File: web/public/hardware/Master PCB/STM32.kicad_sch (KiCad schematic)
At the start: 18 parts, among them SW1 nRST, U1 STM32U585VITx

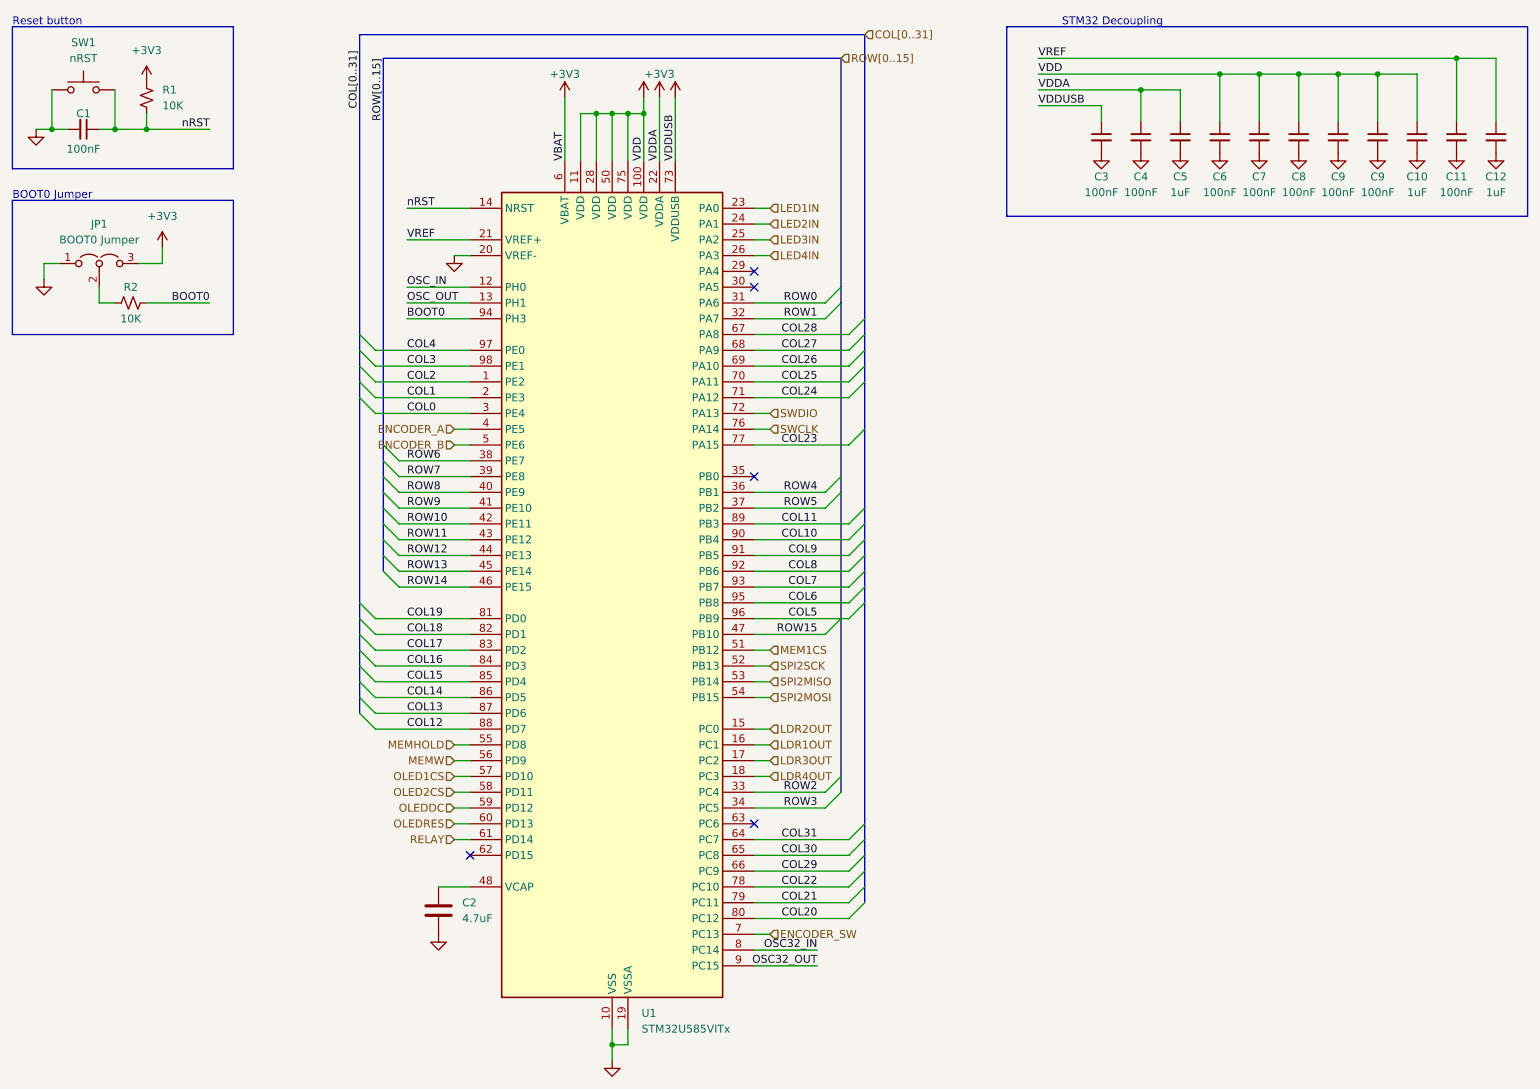
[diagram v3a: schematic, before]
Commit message: Change STM32 pinout, begin placing components on new PCB
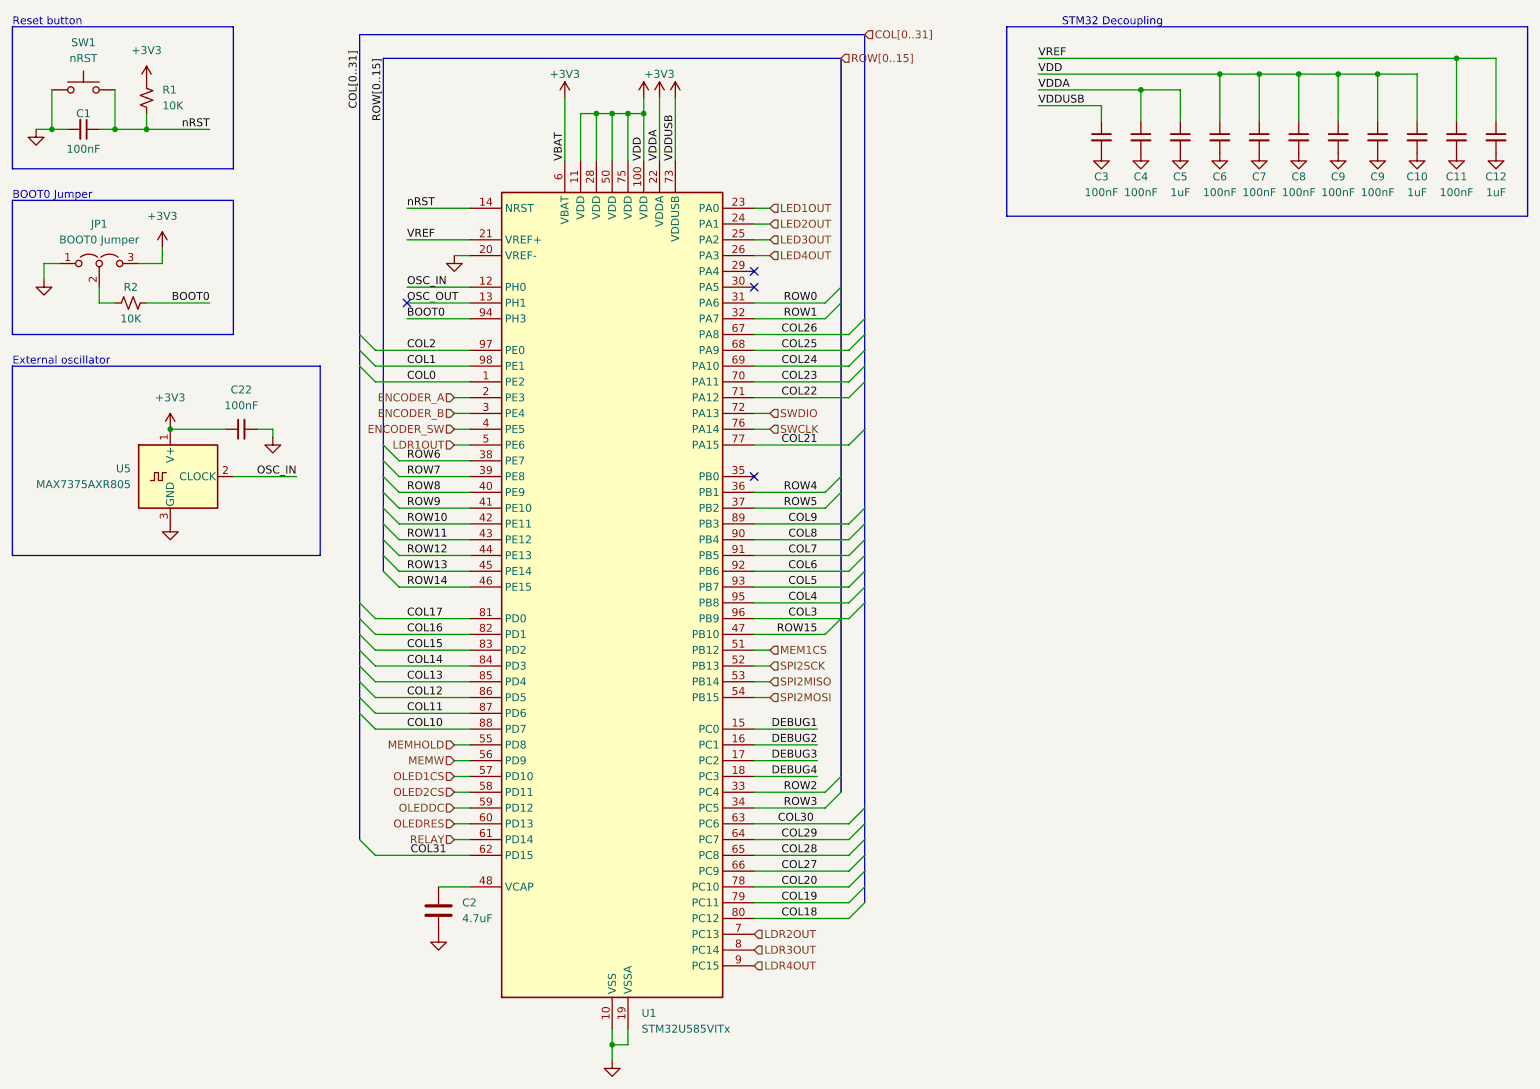
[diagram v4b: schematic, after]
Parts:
- added C22: 100nF, Capacitor_SMD:C_0805_2012Metric_Pad1.18x1.45mm_HandSolder, symbol Device:C_Small
- added U5: MAX7375AXR805, Package_TO_SOT_SMD:SOT-323_SC-70, symbol Oscillator:MAX7375AXR805
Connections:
- net OSC32_IN is gone; now on net LDR3OUT: U1.8 (PC14)
- net OSC32_OUT is gone; now on net LDR4OUT: U1.9 (PC15)
- net +3V3: now also C22.1, U5.1 (V+)
- net COL0: now also U1.1 (PE2); no longer U1.3 (PE4)
- net COL1: now also U1.98 (PE1); no longer U1.2 (PE3)
- net COL10: now also U1.88 (PD7); no longer U1.90 (PB4)
- net COL11: now also U1.87 (PD6); no longer U1.89 (PB3)
- net COL12: now also U1.86 (PD5); no longer U1.88 (PD7)
- net COL13: now also U1.85 (PD4); no longer U1.87 (PD6)
- net COL14: now also U1.84 (PD3); no longer U1.86 (PD5)
- net COL15: now also U1.83 (PD2); no longer U1.85 (PD4)
- net COL16: now also U1.82 (PD1); no longer U1.84 (PD3)
- net COL17: now also U1.81 (PD0); no longer U1.83 (PD2)
- net COL18: now also U1.80 (PC12); no longer U1.82 (PD1)
- net COL19: now also U1.79 (PC11); no longer U1.81 (PD0)
- net COL2: now also U1.97 (PE0); no longer U1.1 (PE2)
- net COL20: now also U1.78 (PC10); no longer U1.80 (PC12)
- net COL21: now also U1.77 (PA15); no longer U1.79 (PC11)
- net COL22: now also U1.71 (PA12); no longer U1.78 (PC10)
- net COL23: now also U1.70 (PA11); no longer U1.77 (PA15)
- net COL24: now also U1.69 (PA10); no longer U1.71 (PA12)
- net COL25: now also U1.68 (PA9); no longer U1.70 (PA11)
- net COL26: now also U1.67 (PA8); no longer U1.69 (PA10)
- net COL27: now also U1.66 (PC9); no longer U1.68 (PA9)
- net COL28: now also U1.65 (PC8); no longer U1.67 (PA8)
- net COL29: now also U1.64 (PC7); no longer U1.66 (PC9)
- net COL3: now also U1.96 (PB9); no longer U1.98 (PE1)
- net COL30: now also U1.63 (PC6); no longer U1.65 (PC8)
- net COL31: now also U1.62 (PD15); no longer U1.64 (PC7)
- net COL4: now also U1.95 (PB8); no longer U1.97 (PE0)
- net COL5: now also U1.93 (PB7); no longer U1.96 (PB9)
- net COL6: now also U1.92 (PB6); no longer U1.95 (PB8)
- net COL7: now also U1.91 (PB5); no longer U1.93 (PB7)
- net COL8: now also U1.90 (PB4); no longer U1.92 (PB6)
- net COL9: now also U1.89 (PB3); no longer U1.91 (PB5)
- net ENCODER_A: now also U1.2 (PE3); no longer U1.4 (PE5)
- net ENCODER_B: now also U1.3 (PE4); no longer U1.5 (PE6)
- net ENCODER_SW: now also U1.4 (PE5); no longer U1.7 (PC13)
- net GND: now also C22.2, U5.3 (GND)
- net LDR1OUT: now also U1.5 (PE6); no longer U1.16 (PC1)
- net LDR2OUT: now also U1.7 (PC13); no longer U1.15 (PC0)
- net LDR3OUT: no longer U1.17 (PC2)
- net LDR4OUT: no longer U1.18 (PC3)
- net OSC_IN: now also U5.2 (CLOCK)
- net LED1IN renamed LED1OUT
- net LED2IN renamed LED2OUT
- net LED3IN renamed LED3OUT
- net LED4IN renamed LED4OUT
- new net DEBUG1: U1.15 (PC0)
- new net DEBUG2: U1.16 (PC1)
- new net DEBUG3: U1.17 (PC2)
- new net DEBUG4: U1.18 (PC3)
- no-connect marks 5 -> 4
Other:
- note added: "External oscillator"

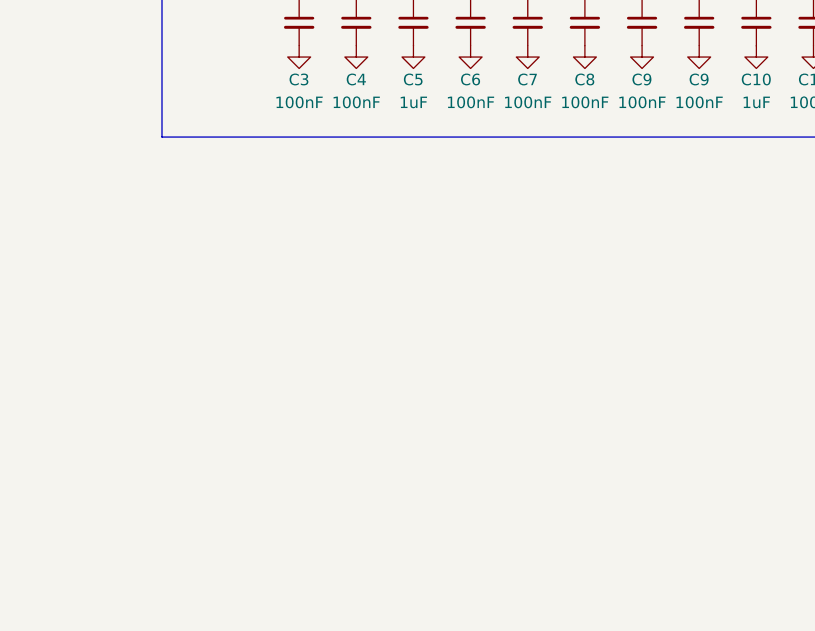
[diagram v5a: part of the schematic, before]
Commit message: Add ESD ICs and route part of board
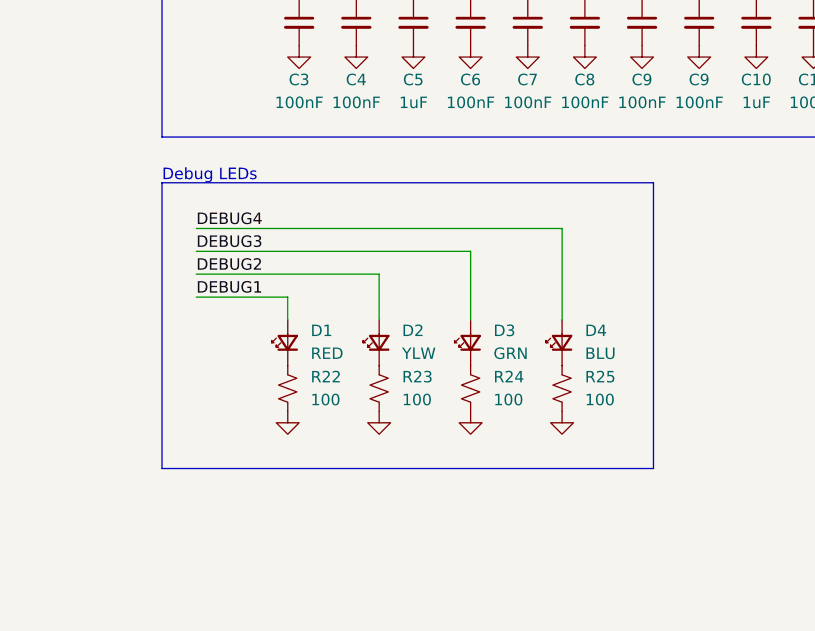
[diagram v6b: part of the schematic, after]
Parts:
- added D1: RED, LED_SMD:LED_0805_2012Metric_Pad1.15x1.40mm_HandSolder, symbol Device:LED_Small
- added D2: YLW, LED_SMD:LED_0805_2012Metric_Pad1.15x1.40mm_HandSolder, symbol Device:LED_Small
- added D3: GRN, LED_SMD:LED_0805_2012Metric_Pad1.15x1.40mm_HandSolder, symbol Device:LED_Small
- added D4: BLU, LED_SMD:LED_0805_2012Metric_Pad1.15x1.40mm_HandSolder, symbol Device:LED_Small
- added R22, R23, R24, R25: 100, Resistor_SMD:R_0805_2012Metric_Pad1.20x1.40mm_HandSolder, symbol Device:R_Small_US
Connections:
- net DEBUG1: now also D1.2 (A)
- net DEBUG2: now also D2.2 (A)
- net DEBUG3: now also D3.2 (A)
- net DEBUG4: now also D4.2 (A)
- net GND: now also R22.2, R23.2, R24.2, R25.2
- new net: D2.1 (K), R23.1
- new net: D4.1 (K), R25.1
- new net: D3.1 (K), R24.1
- new net: D1.1 (K), R22.1
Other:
- note added: "Debug LEDs"

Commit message: Update indicator LED resistor values
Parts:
- R22: value 100 -> 75
- R23: value 100 -> 56
- R24, R25: value 100 -> 0
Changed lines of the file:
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@@
       (effects (font (size 1.27 1.27)) (justify left))
     )
-    (property "Value" "100" (at 214.63 77.47 0)
+    (property "Value" "0" (at 214.63 77.47 0)
       (effects (font (size 1.27 1.27)) (justify left))
     )
@@
       (effects (font (size 1.27 1.27)) (justify left))
     )
-    (property "Value" "100" (at 224.79 77.47 0)
+    (property "Value" "0" (at 224.79 77.47 0)
       (effects (font (size 1.27 1.27)) (justify left))
     )
@@
       (effects (font (size 1.27 1.27)) (justify left))
     )
-    (property "Value" "100" (at 194.31 77.47 0)
+    (property "Value" "75" (at 194.31 77.47 0)
       (effects (font (size 1.27 1.27)) (justify left))
     )
@@
       (effects (font (size 1.27 1.27)) (justify left))
     )
-    (property "Value" "100" (at 204.47 77.47 0)
-      (effects (font (size 1.27 1.27)) (justify left))
-    )
+    (property "Value" "56" (at 204.47 77.47 0)
+      (effects (font (size 1.27 1.27)) (justify left))
+    )

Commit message: Rename nets for clarity
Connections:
- net LDR1OUT renamed LDR1IN
- net LDR2OUT renamed LDR2IN
- net LDR3OUT renamed LDR3IN
- net LDR4OUT renamed LDR4IN
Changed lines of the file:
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@@
     (effects (font (size 1.27 1.27)) (justify right))
   )
-  (hierarchical_label "LDR3OUT" (shape input) (at 137.16 166.37 0) (fields_autoplaced)
+  (hierarchical_label "LDR3IN" (shape input) (at 137.16 166.37 0) (fields_autoplaced)
     (effects (font (size 1.27 1.27)) (justify left))
   )
-  (hierarchical_label "LDR4OUT" (shape input) (at 137.16 168.91 0) (fields_autoplaced)
+  (hierarchical_label "LDR4IN" (shape input) (at 137.16 168.91 0) (fields_autoplaced)
     (effects (font (size 1.27 1.27)) (justify left))
   )
@@
     (effects (font (size 1.27 1.27)) (justify left))
   )
-  (hierarchical_label "LDR2OUT" (shape input) (at 137.16 163.83 0) (fields_autoplaced)
+  (hierarchical_label "LDR2IN" (shape input) (at 137.16 163.83 0) (fields_autoplaced)
     (effects (font (size 1.27 1.27)) (justify left))
   )
@@
     (effects (font (size 1.27 1.27)) (justify right))
   )
-  (hierarchical_label "LDR1OUT" (shape input) (at 88.9 85.09 180) (fields_autoplaced)
+  (hierarchical_label "LDR1IN" (shape input) (at 88.9 85.09 180) (fields_autoplaced)
     (effects (font (size 1.27 1.27)) (justify right))
   )
